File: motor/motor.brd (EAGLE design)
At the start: 62.2 x 53.3 mm, 3 parts

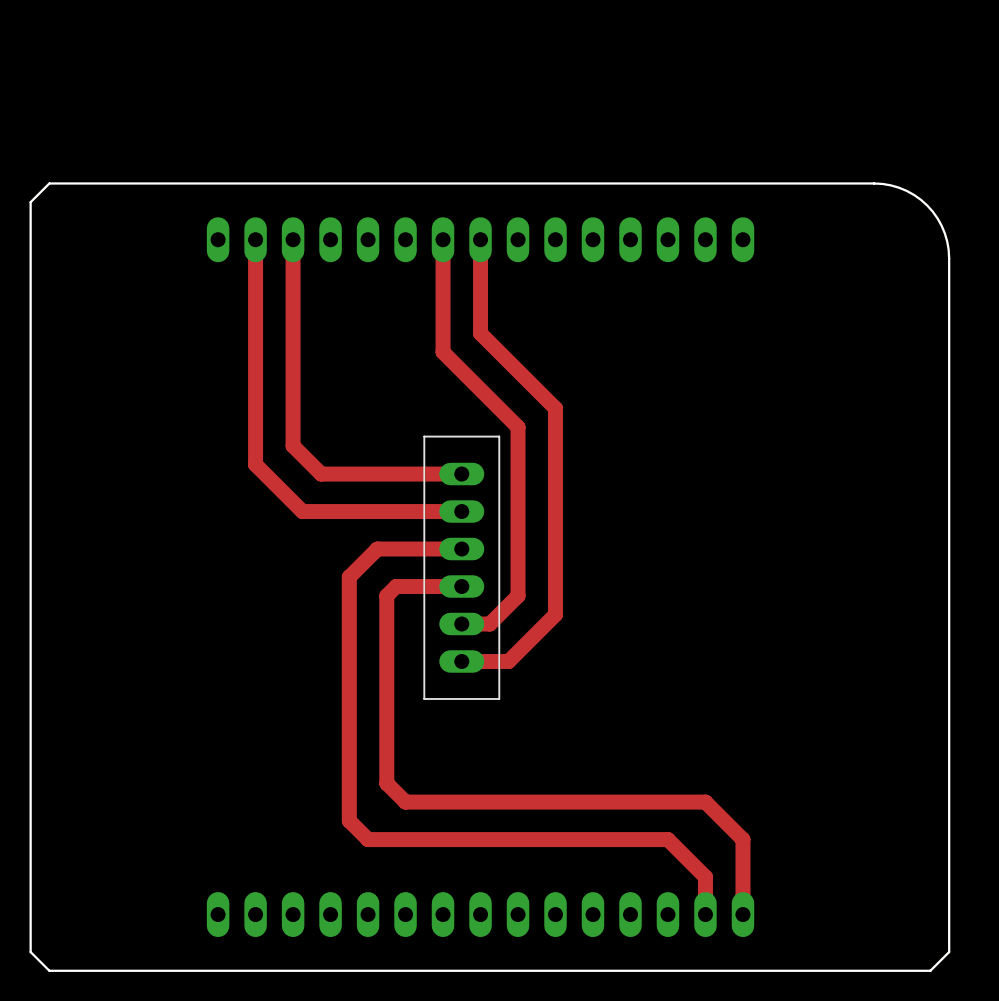
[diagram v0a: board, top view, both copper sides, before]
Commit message: Moved all boards so their bottom left corners are at the origin.
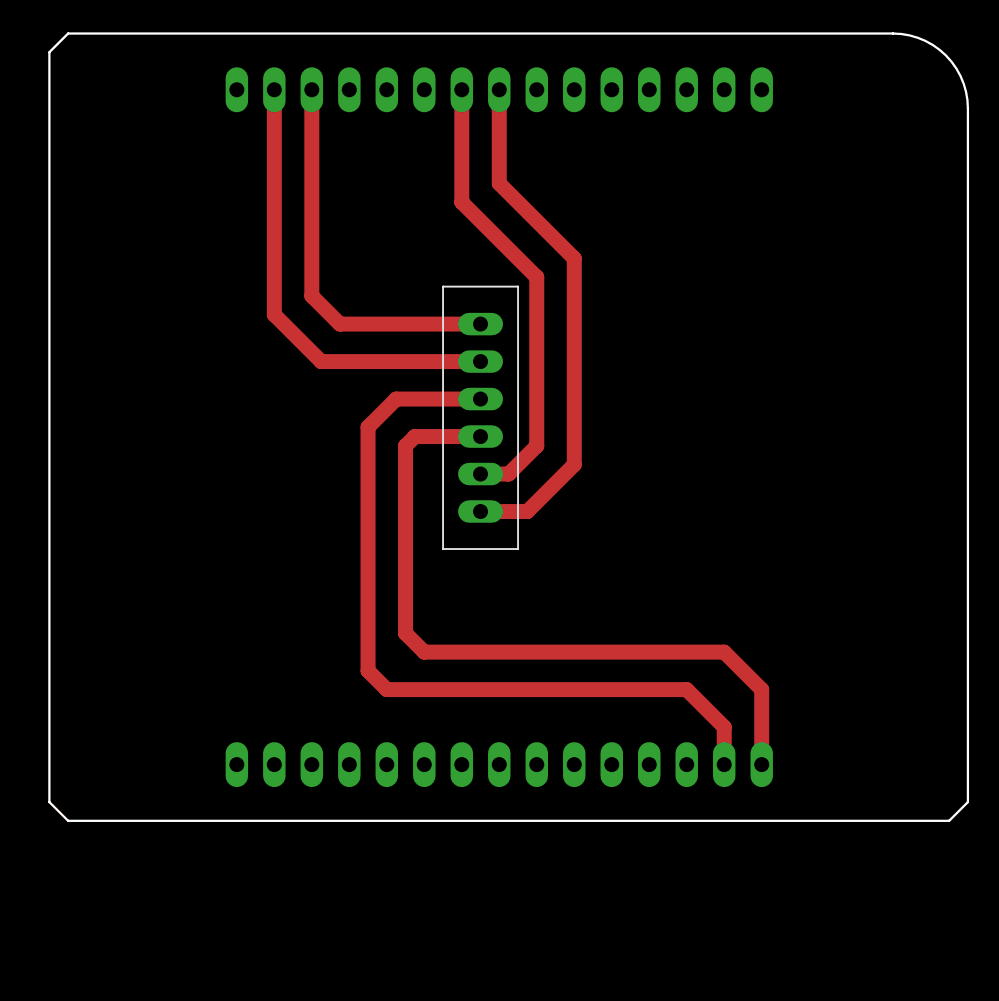
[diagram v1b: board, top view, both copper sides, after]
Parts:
- moved U$1 10.2 mm to (30.5, 49.5)
- moved U$2 10.2 mm to (29.2, 26.0)
- moved U$7 10.2 mm to (30.5, 3.81)
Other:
- outline, holes or cut-outs redrawn
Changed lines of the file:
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@@
 <board>
 <plain>
-<wire x1="0" y1="-10.16" x2="59.69" y2="-10.16" width="0.1524" layer="20"/>
-<wire x1="59.69" y1="-10.16" x2="60.96" y2="-8.89" width="0.1524" layer="20"/>
-<wire x1="60.96" y1="-8.89" x2="60.96" y2="38.1" width="0.1524" layer="20"/>
-<wire x1="60.96" y1="38.1" x2="55.88" y2="43.18" width="0.1524" layer="20" curve="90"/>
-<wire x1="55.88" y1="43.18" x2="0" y2="43.18" width="0.1524" layer="20"/>
-<wire x1="0" y1="43.18" x2="-1.27" y2="41.91" width="0.1524" layer="20"/>
-<wire x1="-1.27" y1="41.91" x2="-1.27" y2="-8.89" width="0.1524" layer="20"/>
-<wire x1="-1.27" y1="-8.89" x2="0" y2="-10.16" width="0.1524" layer="20"/>
+<wire x1="1.27" y1="0" x2="60.96" y2="0" width="0.1524" layer="20"/>
+<wire x1="60.96" y1="0" x2="62.23" y2="1.27" width="0.1524" layer="20"/>
+<wire x1="62.23" y1="1.27" x2="62.23" y2="48.26" width="0.1524" layer="20"/>
+<wire x1="62.23" y1="48.26" x2="57.15" y2="53.34" width="0.1524" layer="20" curve="90"/>
+<wire x1="57.15" y1="53.34" x2="1.27" y2="53.34" width="0.1524" layer="20"/>
+<wire x1="1.27" y1="53.34" x2="0" y2="52.07" width="0.1524" layer="20"/>
+<wire x1="0" y1="52.07" x2="0" y2="1.27" width="0.1524" layer="20"/>
+<wire x1="0" y1="1.27" x2="1.27" y2="0" width="0.1524" layer="20"/>
 </plain>
 <attributes>
@@
 </autorouter>
 <elements>
-<element name="U$1" library="RC Car" package="ARDUINO-NANO-JUMPER-1" value="ARDUINO-NANO-JUMPER-1" x="29.21" y="39.37" smashed="yes"/>
-<element name="U$2" library="RC Car" package="L9100S" value="L9110S" x="27.94" y="15.875" smashed="yes" rot="R270"/>
-<element name="U$7" library="RC Car" package="ARDUINO-NANO-JUMPER-2" value="ARDUINO-NANO-JUMPER-2" x="29.21" y="-6.35" smashed="yes"/>
+<element name="U$1" library="RC Car" package="ARDUINO-NANO-JUMPER-1" value="ARDUINO-NANO-JUMPER-1" x="30.48" y="49.53" smashed="yes"/>
+<element name="U$2" library="RC Car" package="L9100S" value="L9110S" x="29.21" y="26.035" smashed="yes" rot="R270"/>
+<element name="U$7" library="RC Car" package="ARDUINO-NANO-JUMPER-2" value="ARDUINO-NANO-JUMPER-2" x="30.48" y="3.81" smashed="yes"/>
 </elements>
 <signals>
@@
 <contactref element="U$1" pad="D6"/>
 <contactref element="U$2" pad="A-1A"/>
-<wire x1="26.67" y1="31.75" x2="31.75" y2="26.67" width="1.016" layer="1"/>
-<wire x1="31.75" y1="26.67" x2="31.75" y2="15.24" width="1.016" layer="1"/>
-<wire x1="29.845" y1="13.335" x2="27.94" y2="13.335" width="1.016" layer="1"/>
-<wire x1="26.67" y1="39.37" x2="26.67" y2="31.75" width="1.016" layer="1"/>
-<wire x1="31.75" y1="15.24" x2="29.845" y2="13.335" width="1.016" layer="1"/>
+<wire x1="27.94" y1="41.91" x2="33.02" y2="36.83" width="1.016" layer="1"/>
+<wire x1="33.02" y1="36.83" x2="33.02" y2="25.4" width="1.016" layer="1"/>
+<wire x1="31.115" y1="23.495" x2="29.21" y2="23.495" width="1.016" layer="1"/>
+<wire x1="27.94" y1="49.53" x2="27.94" y2="41.91" width="1.016" layer="1"/>
+<wire x1="33.02" y1="25.4" x2="31.115" y2="23.495" width="1.016" layer="1"/>
 </signal>
 <signal name="D05">
 <contactref element="U$1" pad="D5"/>
 <contactref element="U$2" pad="A-1B"/>
-<wire x1="29.21" y1="39.37" x2="29.21" y2="33.02" width="1.016" layer="1"/>
-<wire x1="29.21" y1="33.02" x2="34.29" y2="27.94" width="1.016" layer="1"/>
-<wire x1="31.115" y1="10.795" x2="27.94" y2="10.795" width="1.016" layer="1"/>
-<wire x1="34.29" y1="27.94" x2="34.29" y2="13.97" width="1.016" layer="1"/>
-<wire x1="34.29" y1="13.97" x2="31.115" y2="10.795" width="1.016" layer="1"/>
+<wire x1="30.48" y1="49.53" x2="30.48" y2="43.18" width="1.016" layer="1"/>
+<wire x1="30.48" y1="43.18" x2="35.56" y2="38.1" width="1.016" layer="1"/>
+<wire x1="32.385" y1="20.955" x2="29.21" y2="20.955" width="1.016" layer="1"/>
+<wire x1="35.56" y1="38.1" x2="35.56" y2="24.13" width="1.016" layer="1"/>
+<wire x1="35.56" y1="24.13" x2="32.385" y2="20.955" width="1.016" layer="1"/>
 </signal>
 <signal name="N$1">
 <contactref element="U$2" pad="GND"/>
 <contactref element="U$7" pad="GND"/>
-<wire x1="44.45" y1="-6.35" x2="44.45" y2="-3.81" width="1.016" layer="1"/>
-<wire x1="41.91" y1="-1.27" x2="21.59" y2="-1.27" width="1.016" layer="1"/>
-<wire x1="21.59" y1="-1.27" x2="20.32" y2="0" width="1.016" layer="1"/>
-<wire x1="20.32" y1="0" x2="20.32" y2="16.51" width="1.016" layer="1"/>
-<wire x1="22.225" y1="18.415" x2="27.94" y2="18.415" width="1.016" layer="1"/>
-<wire x1="44.45" y1="-3.81" x2="41.91" y2="-1.27" width="1.016" layer="1"/>
-<wire x1="20.32" y1="16.51" x2="22.225" y2="18.415" width="1.016" layer="1"/>
+<wire x1="45.72" y1="3.81" x2="45.72" y2="6.35" width="1.016" layer="1"/>
+<wire x1="43.18" y1="8.89" x2="22.86" y2="8.89" width="1.016" layer="1"/>
+<wire x1="22.86" y1="8.89" x2="21.59" y2="10.16" width="1.016" layer="1"/>
+<wire x1="21.59" y1="10.16" x2="21.59" y2="26.67" width="1.016" layer="1"/>
+<wire x1="23.495" y1="28.575" x2="29.21" y2="28.575" width="1.016" layer="1"/>
+<wire x1="45.72" y1="6.35" x2="43.18" y2="8.89" width="1.016" layer="1"/>
+<wire x1="21.59" y1="26.67" x2="23.495" y2="28.575" width="1.016" layer="1"/>
 </signal>
 <signal name="N$2">
 <contactref element="U$7" pad="VIN"/>
 <contactref element="U$2" pad="VCC"/>
-<wire x1="46.99" y1="-6.35" x2="46.99" y2="-1.27" width="1.016" layer="1"/>
-<wire x1="46.99" y1="-1.27" x2="44.45" y2="1.27" width="1.016" layer="1"/>
-<wire x1="24.13" y1="1.27" x2="22.86" y2="2.54" width="1.016" layer="1"/>
-<wire x1="22.86" y1="2.54" x2="22.86" y2="15.24" width="1.016" layer="1"/>
-<wire x1="22.86" y1="15.24" x2="23.495" y2="15.875" width="1.016" layer="1"/>
-<wire x1="23.495" y1="15.875" x2="27.94" y2="15.875" width="1.016" layer="1"/>
-<wire x1="44.45" y1="1.27" x2="24.13" y2="1.27" width="1.016" layer="1"/>
+<wire x1="48.26" y1="3.81" x2="48.26" y2="8.89" width="1.016" layer="1"/>
+<wire x1="48.26" y1="8.89" x2="45.72" y2="11.43" width="1.016" layer="1"/>
+<wire x1="25.4" y1="11.43" x2="24.13" y2="12.7" width="1.016" layer="1"/>
+<wire x1="24.13" y1="12.7" x2="24.13" y2="25.4" width="1.016" layer="1"/>
+<wire x1="24.13" y1="25.4" x2="24.765" y2="26.035" width="1.016" layer="1"/>
+<wire x1="24.765" y1="26.035" x2="29.21" y2="26.035" width="1.016" layer="1"/>
+<wire x1="45.72" y1="11.43" x2="25.4" y2="11.43" width="1.016" layer="1"/>
 </signal>
 <signal name="N$3">
 <contactref element="U$2" pad="B-2A"/>
 <contactref element="U$1" pad="D11"/>
-<wire x1="17.145" y1="20.955" x2="27.94" y2="20.955" width="1.016" layer="1"/>
-<wire x1="13.97" y1="39.37" x2="13.97" y2="24.13" width="1.016" layer="1"/>
-<wire x1="13.97" y1="24.13" x2="17.145" y2="20.955" width="1.016" layer="1"/>
+<wire x1="18.415" y1="31.115" x2="29.21" y2="31.115" width="1.016" layer="1"/>
+<wire x1="15.24" y1="49.53" x2="15.24" y2="34.29" width="1.016" layer="1"/>
+<wire x1="15.24" y1="34.29" x2="18.415" y2="31.115" width="1.016" layer="1"/>
 </signal>
 <signal name="N$4">
 <contactref element="U$1" pad="D10"/>
 <contactref element="U$2" pad="B-1A"/>
-<wire x1="16.51" y1="39.37" x2="16.51" y2="25.4" width="1.016" layer="1"/>
-<wire x1="18.415" y1="23.495" x2="27.94" y2="23.495" width="1.016" layer="1"/>
-<wire x1="16.51" y1="25.4" x2="18.415" y2="23.495" width="1.016" layer="1"/>
+<wire x1="17.78" y1="49.53" x2="17.78" y2="35.56" width="1.016" layer="1"/>
+<wire x1="19.685" y1="33.655" x2="29.21" y2="33.655" width="1.016" layer="1"/>
+<wire x1="17.78" y1="35.56" x2="19.685" y2="33.655" width="1.016" layer="1"/>
 </signal>
 </signals>

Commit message: Fixed board lengths for motor and power boards.
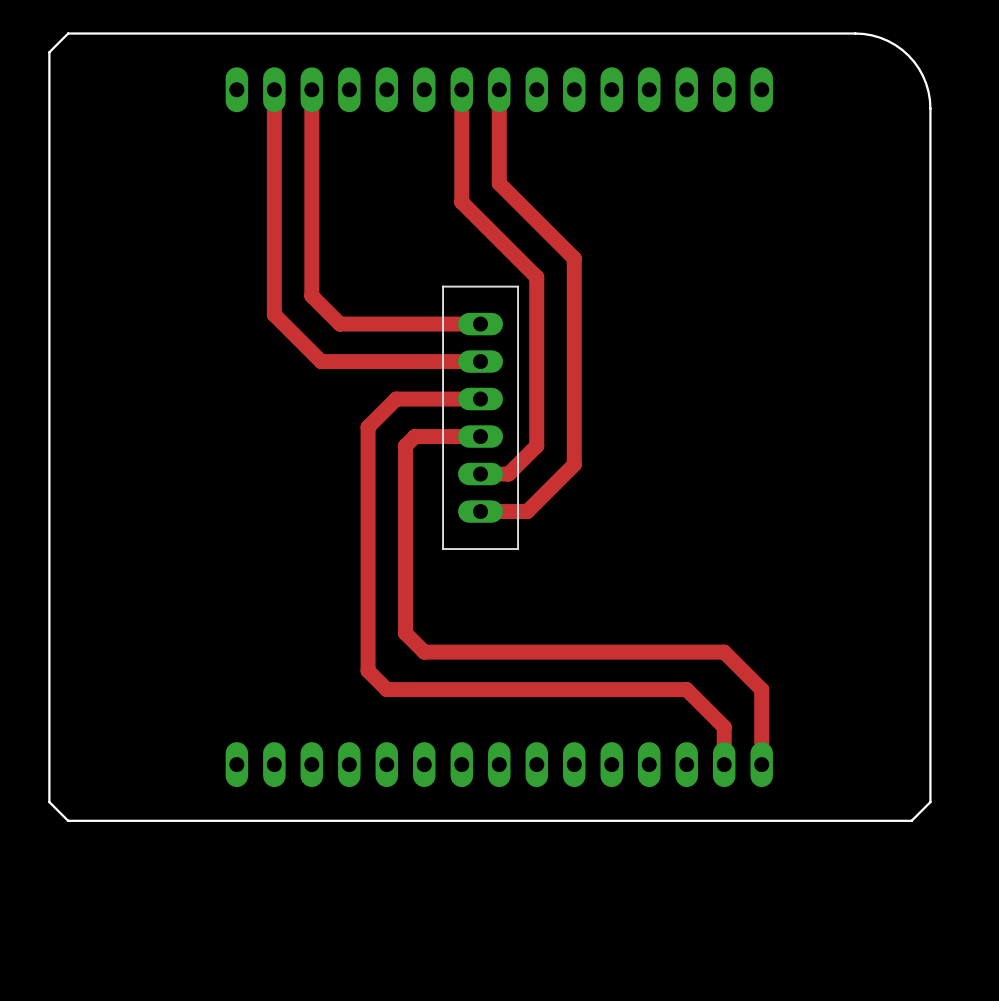
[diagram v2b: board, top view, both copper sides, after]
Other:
- board size 62.2 x 53.3 mm -> 59.7 x 53.3 mm
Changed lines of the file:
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@@
 <board>
 <plain>
-<wire x1="1.27" y1="0" x2="60.96" y2="0" width="0.1524" layer="20"/>
-<wire x1="60.96" y1="0" x2="62.23" y2="1.27" width="0.1524" layer="20"/>
-<wire x1="62.23" y1="1.27" x2="62.23" y2="48.26" width="0.1524" layer="20"/>
-<wire x1="62.23" y1="48.26" x2="57.15" y2="53.34" width="0.1524" layer="20" curve="90"/>
-<wire x1="57.15" y1="53.34" x2="1.27" y2="53.34" width="0.1524" layer="20"/>
+<wire x1="1.27" y1="0" x2="58.42" y2="0" width="0.1524" layer="20"/>
+<wire x1="58.42" y1="0" x2="59.69" y2="1.27" width="0.1524" layer="20"/>
+<wire x1="59.69" y1="1.27" x2="59.69" y2="48.26" width="0.1524" layer="20"/>
+<wire x1="59.69" y1="48.26" x2="54.61" y2="53.34" width="0.1524" layer="20" curve="90"/>
+<wire x1="54.61" y1="53.34" x2="1.27" y2="53.34" width="0.1524" layer="20"/>
 <wire x1="1.27" y1="53.34" x2="0" y2="52.07" width="0.1524" layer="20"/>
 <wire x1="0" y1="52.07" x2="0" y2="1.27" width="0.1524" layer="20"/>

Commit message: Updated Boards for New Configuration
Bluetooth board has been rearranged to accommodate board slot-in
Motor Control Board flipped to be in the right spot
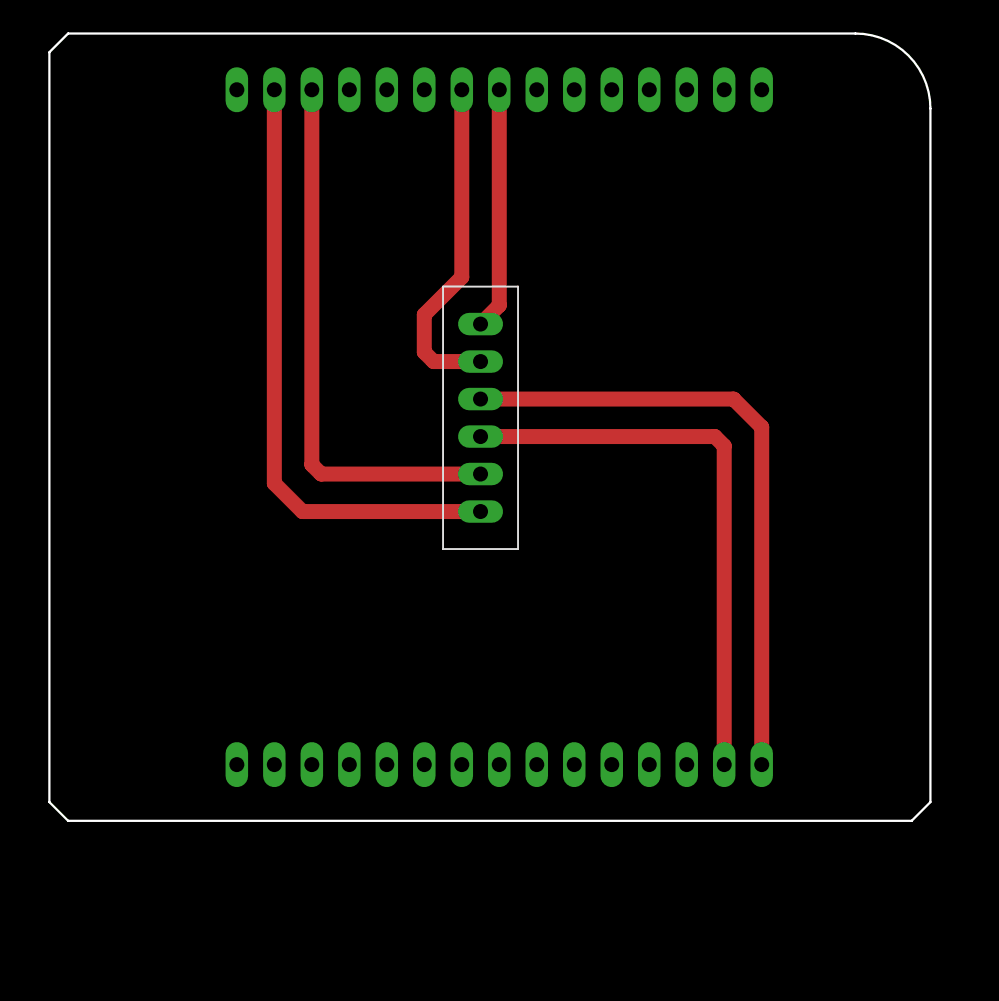
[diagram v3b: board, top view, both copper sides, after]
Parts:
- moved U$2 2.54 mm to (29.2, 28.6), turned to 90 degrees
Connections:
- new net N$5: U$2.B-1A
- net N$3: now also U$2.B-1A; no longer U$2.B-2A
- net N$4: now also U$2.B-2A; no longer U$2.B-1A
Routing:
- net D05: track 35.2 -> 16.4 mm
- net N$1: track 53.2 -> 38.4 mm
- net N$4: track 26.2 -> 37.1 mm
- net N$3: track 30.5 -> 41.4 mm
- net D06: track 30.8 -> 22.9 mm
- net N$2: track 48.8 -> 42.7 mm

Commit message: Added breadboard board. This commit is going to production.
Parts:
- moved U$1 45.7 mm to (30.5, 3.81), turned to 180 degrees
- moved U$7 45.7 mm to (30.5, 49.5), turned to 180 degrees
- moved U$2 12.0 mm to (17.8, 24.8), turned to 270 degrees
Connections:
- net N$1 renamed GND
- net N$2 renamed VIN
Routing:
- net VIN: track 42.7 -> 28.4 mm
- net GND: track 38.4 -> 24.1 mm
- net N$3: track 41.4 -> 55.0 mm
- net N$4: track 37.1 -> 49.9 mm
- net D05: track 16.4 -> 27.1 mm
- net D06: track 22.9 -> 32.2 mm
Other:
- board text added: "3V3"
- board text added: "5V"
- board text added: "A-1A"
- board text added: "A-1B"
- board text added: "B-1A"
- board text added: "B-2A"
- board text added: "BOARD ON THIS SIDE"
- board text added: "GND"
- board text added: "RC CARS MOTOR BOARD v0.1"
- board text added: "VCC"
- board text added: "VIN"
